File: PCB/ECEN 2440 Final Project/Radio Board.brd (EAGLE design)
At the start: 41.6 x 57.1 mm, 14 parts

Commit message: Final updates to the board
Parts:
- removed U$5: LDO-S-816, Custom Library:LDO-S-816
- added 3V3POWER: (no value), pinhead:1X02
- added LM317: LM317, Custom Library:LM317
- added R4, R5: 100R, rcl:R0805
- moved X1 33.1 mm to (12.7, 85.1)
- moved U$6 31.9 mm to (8.89, 74.9)
- moved U$4 7.73 mm to (5.08, 11.4)
- renumbered JP2 to RADIO, JP3 to BATTERYPOWER
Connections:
- new net N$8: LM317.ADJUST1, R4.1
- net +3V3: now also 3V3POWER.1, LM317.VOUT, R4.2, R5.1
- net GND: now also 3V3POWER.2, R5.2; no longer U$5.VSS
- net VCC: now also LM317.VIN; no longer U$5.VIN
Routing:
- net GND: track 0.00 -> 184.1 mm
- net +3V3: track 0.00 -> 119.0 mm
- net VCC: track 0.00 -> 66.5 mm
- net N$3: track 0.00 -> 48.1 mm, vias 0 -> 1
- net N$1: track 0.00 -> 39.9 mm
- net AUDIO_PWM: track 0.00 -> 38.0 mm
- net AUDIO_PTT: track 0.00 -> 26.4 mm
- net N$5: track 0.00 -> 17.2 mm
- net N$8: track 0.00 -> 14.1 mm
- net N$2: track 0.00 -> 13.0 mm
- net N$4: track 0.00 -> 13.0 mm
- net N$6: track 0.00 -> 10.4 mm
- net RX_RADIO: track 0.00 -> 9.01 mm
- net TX_RADIO: track 0.00 -> 7.14 mm
- net GND1: track 0.00 -> 3.19 mm
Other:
- board size 41.6 x 57.1 mm -> 44.1 x 86.3 mm

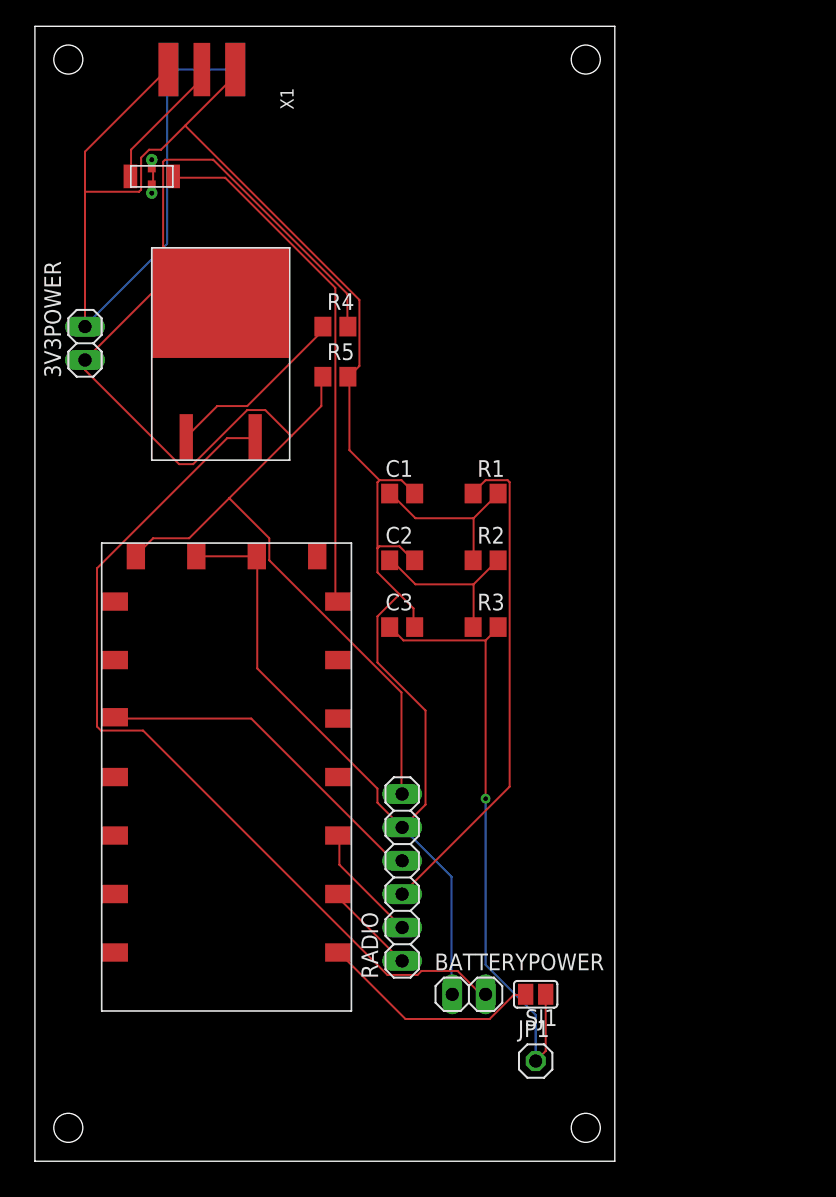
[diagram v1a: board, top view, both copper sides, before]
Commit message: radio board routing
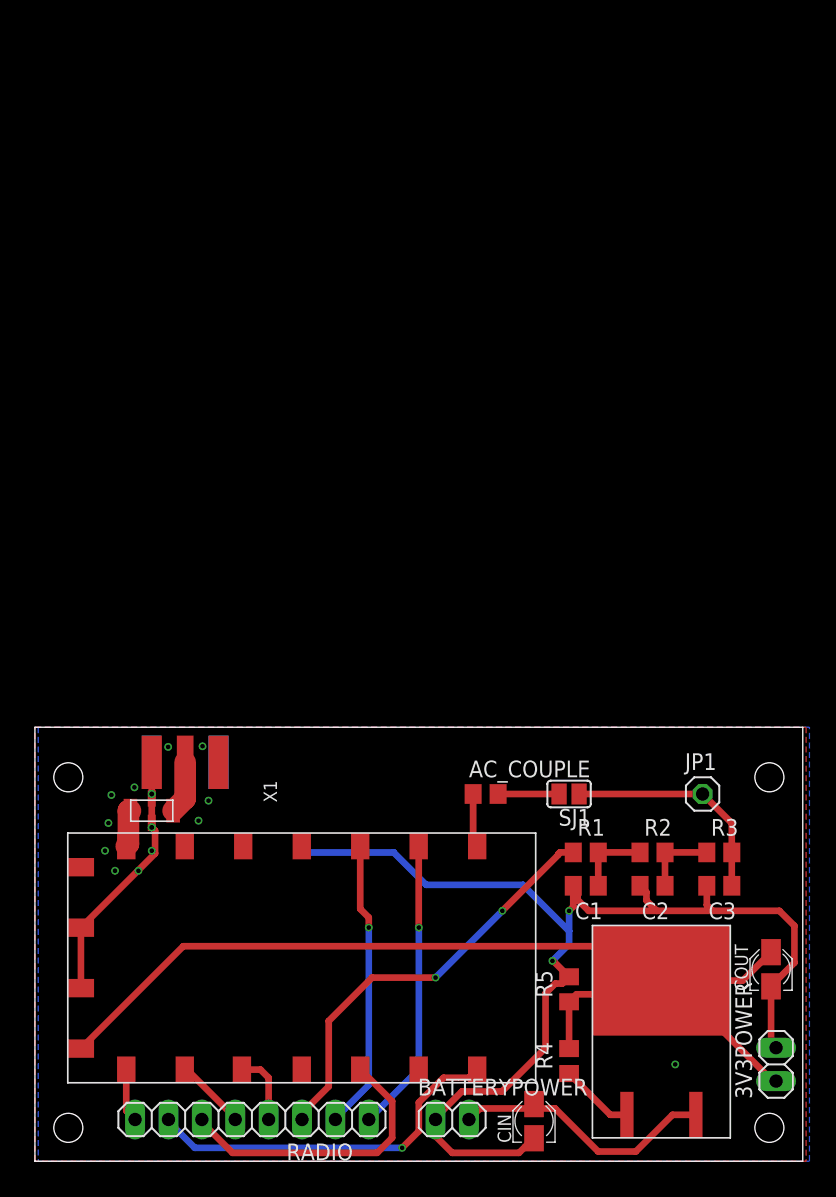
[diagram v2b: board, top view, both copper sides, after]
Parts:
- added AC_COUPLE: 1u, rcl:C0805
- added CIN: 100nF, rcl:PANASONIC_A
- added COUT: 1uF, rcl:PANASONIC_A
- R4: value 100R -> 220R
- R5: value 100R -> 470R
- RADIO: device pinhead:1X06 -> pinhead:1X08
- moved 3V3POWER 76.0 mm to (56.4, 7.37)
- moved LM317 61.5 mm to (42.4, 1.78)
- moved R4 58.6 mm to (40.6, 7.62), turned to 90 degrees
- moved X1 52.7 mm to (11.4, 32.4)
- moved R5 49.9 mm to (40.6, 13.1), turned to 90 degrees
- moved U$6 48.3 mm to (8.89, 26.7), turned to 0 degrees
- moved U$4 33.5 mm to (38.1, 5.97), turned to 90 degrees
- moved C1 33.0 mm to (41.9, 21.0), turned to 180 degrees
- moved C2 31.2 mm to (47.0, 21.0), turned to 180 degrees
- moved C3 31.1 mm to (52.1, 21.0), turned to 180 degrees
- moved R1 28.3 mm to (41.9, 23.5)
- moved R2 25.6 mm to (47.0, 23.5)
- moved R3 24.7 mm to (52.1, 23.5)
- moved JP1 24.0 mm to (50.8, 27.9)
- moved RADIO 21.7 mm to (16.5, 3.17), turned to 180 degrees
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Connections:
- removed net GND1: U$6.GND1, U$6.GND2, U$6.P$1, U$6.P$2
- new net AF_OUT: RADIO.6, U$4.AF_OUT
- new net H/L: RADIO.8, U$4.H/L
- new net N$7: AC_COUPLE.2, SJ1.2
- new net PD: RADIO.5, U$4.PD
- new net SQ: RADIO.7, U$4.SQ
- net +3V3: now also COUT.+; no longer RADIO.6
- net GND: now also CIN.-, COUT.-, U$6.GND1, U$6.GND2, U$6.P$1, U$6.P$2; no longer RADIO.5
- net N$5: now also AC_COUPLE.1; no longer SJ1.2
- net VCC: now also CIN.+
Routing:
- net GND: track 184.1 -> 111.8 mm, vias 0 -> 14
- net VCC: track 66.5 -> 20.6 mm
- net +3V3: track 119.0 -> 80.5 mm
- net N$1: track 39.9 -> 2.92 mm
- net N$3: track 48.1 -> 17.3 mm, vias 1 -> 0
- net SQ: track 0.00 -> 28.2 mm, vias 0 -> 1
- net AF_OUT: track 0.00 -> 22.3 mm
- net AUDIO_PTT: track 26.4 -> 5.46 mm
- net TX_RADIO: track 7.14 -> 22.4 mm, vias 0 -> 1
- net RX_RADIO: track 9.01 -> 22.1 mm, vias 0 -> 1
- net N$5: track 17.2 -> 4.10 mm
- net N$8: track 14.1 -> 5.70 mm
- net N$2: track 13.0 -> 5.72 mm
- net N$4: track 13.0 -> 5.72 mm
- net N$6: track 10.4 -> 4.06 mm
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- added copper zone on layer 1, net GND
- added copper zone on layer 16, net GND
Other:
- board size 44.1 x 86.3 mm -> 58.4 x 33 mm

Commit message: final (before review & order) dra818v breakout board
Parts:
- moved SJ1 3.56 mm to (44.2, 27.9)
- moved AC_COUPLE 2.03 mm to (36.3, 27.9)
- renumbered BATTERYPOWER to BATT
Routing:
- net GND: track 111.8 -> 119.5 mm
- net AUDIO_PWM: track 32.3 -> 35.2 mm
- net N$7: track 4.64 -> 6.16 mm
- net N$3: track 17.3 -> 15.9 mm
- net N$5: track 4.10 -> 5.30 mm
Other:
- board text added: "+"
- board text added: "aout"
- board text added: "h/l"
- board text added: "mic"
- board text added: "pd"
- board text added: "ptt"
- board text added: "rx"
- board text added: "sq"
- board text added: "tx"

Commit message: final (i hope) radio board
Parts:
- removed 3V3POWER: (no value), pinhead:1X02
- removed LM317: LM317, Custom Library:LM317
- added 4VPWR: (no value), pinhead:1X02
- added C4: 500n, rcl:C0805
- added CIN1, CIN2: (no value), rcl:PANASONIC_A
- added L1: (no value), rcl:L3225M
- added R6: 0R, rcl:R0805
- added R8, R9: (no value), rcl:R0805
- added U$1: BD00COAW, Custom Library:HRP5
- R4: value 220R -> 43k
- R5: value 470R -> 10k
- moved COUT 52.5 mm to (3.56, 17.7), turned to 180 degrees
- moved CIN 44.5 mm to (7.11, 35.1), turned to 270 degrees
- moved BATT 43.2 mm to (2.67, 35.1), turned to 270 degrees
- moved R4 41.0 mm to (2.54, 22.9), flipped to the bottom, turned to 180 degrees
- moved R5 40.5 mm to (2.54, 26.7), flipped to the bottom, turned to 180 degrees
- moved RADIO 21.6 mm to (38.1, 3.17)
- moved C3 17.2 mm to (34.9, 22.2), flipped to the bottom, turned to 0 degrees
- moved U$4 16.7 mm to (54.7, 7.37)
- moved U$6 15.2 mm to (23.6, 30.2), turned to 90 degrees
- moved AC_COUPLE 14.3 mm to (50.2, 31.4), turned to 90 degrees
- moved R3 13.5 mm to (38.7, 21.6), flipped to the bottom, turned to 90 degrees
- moved X1 13.3 mm to (23.6, 37.7)
- moved R1 12.5 mm to (38.7, 11.4), flipped to the bottom, turned to 90 degrees
- moved C2 12.3 mm to (35.2, 17.5), flipped to the bottom, turned to 0 degrees
- moved C1 11.4 mm to (34.5, 12.3), flipped to the bottom, turned to 0 degrees
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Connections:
- removed net +3V3: 3V3POWER.1, COUT.+, LM317.VOUT, R4.2, R5.1, U$4.VBAT
- new net ADJ: R4.2, R5.1, U$1.5
- new net GNDA: R6.1, U$6.GND1, U$6.GND2, U$6.P$1, U$6.P$2, X1.GND@1, X1.GND@2, X1.GND@3, X1.GND@4
- new net N$9: CIN1.+, R8.2
- new net V+: 4VPWR.1, C4.1, L1.2, R8.1, R9.1, U$4.VBAT
- new net VO: COUT.+, L1.1, R4.1, U$1.4
- net GND: now also 4VPWR.2, C4.2, CIN1.-, CIN2.-, R6.2, U$1.3, U$1.6; no longer 3V3POWER.2, U$6.GND1, U$6.GND2, U$6.P$1, U$6.P$2, X1.GND@1, X1.GND@2, X1.GND@3, X1.GND@4
- net N$8: now also CIN2.+, R9.2; no longer LM317.ADJUST1, R4.1
- net VCC: now also U$1.1, U$1.2; no longer LM317.VIN
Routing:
- net GND: track 119.5 -> 0.00 mm, vias 14 -> 10
- net +3V3: track 80.5 -> 0.00 mm
- net AUDIO_PWM: track 35.2 -> 8.62 mm, vias 2 -> 0
- net V+: track 0.00 -> 24.7 mm
- net VO: track 0.00 -> 16.6 mm, vias 0 -> 1
- net AF_OUT: track 22.3 -> 9.92 mm, vias 0 -> 1
- net ADJ: track 0.00 -> 10.1 mm, vias 0 -> 1
- net VCC: track 20.6 -> 11.0 mm
- net PD: track 5.49 -> 11.4 mm
- net AUDIO_PTT: track 5.46 -> 9.80 mm
- net H/L: track 4.07 -> 7.77 mm
- net N$8: track 5.70 -> 2.83 mm
- net N$9: track 0.00 -> 2.83 mm
- net SQ: track 28.2 -> 26.4 mm, vias 1 -> 0
- net N$3: track 15.9 -> 17.7 mm
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- added copper zone on layer 1, net GNDA
- added copper zone on layer 16, net GNDA
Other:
- board size 58.4 x 33 mm -> 58.4 x 38.1 mm

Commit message: final board maybe??
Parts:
- U$1: value BD00COAW -> BDXXC0A-CBD00C0AWHFP-CTR
- moved U$1 0.65 mm to (7.62, 25.7)
- moved CIN 0.65 mm to (6.48, 35.2)
- moved C4 0.52 mm to (16.4, 10.9)
- moved R9 0.52 mm to (8.76, 10.9)
- moved R8 0.52 mm to (12.6, 10.9)
- moved R6 0.38 mm to (16.3, 35.4)
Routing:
- net ADJ: track 10.1 -> 8.33 mm
- net AUDIO_PTT: track 9.80 -> 10.6 mm, vias 0 -> 1
- net V+: track 24.7 -> 24.1 mm
- net VCC: track 11.0 -> 10.4 mm
- net N$8: track 2.83 -> 3.39 mm
- net N$9: track 2.83 -> 3.39 mm
- net SQ: track 26.4 -> 25.9 mm
- net N$5: track 5.10 -> 4.60 mm
- net N$1: track 3.25 -> 2.75 mm

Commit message: naming
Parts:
- C1, C2, C3: value 500n -> (none)
- R1, R2, R3: value 100R -> 0R
- renumbered CIN1 to C5, CIN2 to C6
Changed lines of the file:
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@@
 <setting verticaltext="up"/>
 </settings>
-<grid distance="0.05" unitdist="inch" unit="mil" style="lines" multiple="1" display="yes" altdistance="5" altunitdist="mil" altunit="inch"/>
+<grid distance="0.05" unitdist="inch" unit="mm" style="lines" multiple="1" display="yes" altdistance="5" altunitdist="mil" altunit="inch"/>
 <layers>
 <layer number="1" name="Top" color="4" fill="1" visible="yes" active="yes"/>
@@
 </autorouter>
 <elements>
-<element name="C1" library="rcl" library_urn="urn:adsk.eagle:library:334" package="C0805" package3d_urn="urn:adsk.eagle:package:23617/2" value="500n" x="34.544" y="12.319" smashed="yes" rot="MR0">
+<element name="C1" library="rcl" library_urn="urn:adsk.eagle:library:334" package="C0805" package3d_urn="urn:adsk.eagle:package:23617/2" value="" x="34.544" y="12.319" smashed="yes" rot="MR0">
 <attribute name="NAME" x="35.814" y="13.589" size="1.27" layer="26" rot="MR0"/>
 <attribute name="POPULARITY" value="63" x="-2.286" y="-28.321" size="1.778" layer="28" rot="MR0" display="off"/>
@@
 <attribute name="VALUE" x="35.814" y="9.779" size="1.27" layer="28" rot="MR0"/>
 </element>
-<element name="C2" library="rcl" library_urn="urn:adsk.eagle:library:334" package="C0805" package3d_urn="urn:adsk.eagle:package:23617/2" value="500n" x="35.179" y="17.526" smashed="yes" rot="MR0">
+<element name="C2" library="rcl" library_urn="urn:adsk.eagle:library:334" package="C0805" package3d_urn="urn:adsk.eagle:package:23617/2" value="" x="35.179" y="17.526" smashed="yes" rot="MR0">
 <attribute name="NAME" x="36.449" y="18.796" size="1.27" layer="26" rot="MR0"/>
 <attribute name="POPULARITY" value="63" x="-8.001" y="-23.114" size="1.778" layer="28" rot="MR0" display="off"/>
@@
 <attribute name="VALUE" x="36.449" y="14.986" size="1.27" layer="28" rot="MR0"/>
 </element>
-<element name="C3" library="rcl" library_urn="urn:adsk.eagle:library:334" package="C0805" package3d_urn="urn:adsk.eagle:package:23617/2" value="500n" x="34.925" y="22.225" smashed="yes" rot="MR0">
+<element name="C3" library="rcl" library_urn="urn:adsk.eagle:library:334" package="C0805" package3d_urn="urn:adsk.eagle:package:23617/2" value="" x="34.925" y="22.225" smashed="yes" rot="MR0">
 <attribute name="NAME" x="36.195" y="23.495" size="1.27" layer="26" rot="MR0"/>
 <attribute name="POPULARITY" value="63" x="18.415" y="-24.765" size="1.778" layer="28" rot="MR0" display="off"/>
@@
 <attribute name="VALUE" x="45.72" y="6.35" size="1.27" layer="27" rot="R180"/>
 </element>
-<element name="R1" library="rcl" library_urn="urn:adsk.eagle:library:334" package="R0805" package3d_urn="urn:adsk.eagle:package:23553/2" value="100R" x="38.735" y="11.43" smashed="yes" rot="MR90">
+<element name="R1" library="rcl" library_urn="urn:adsk.eagle:library:334" package="R0805" package3d_urn="urn:adsk.eagle:package:23553/2" value="0R" x="38.735" y="11.43" smashed="yes" rot="MR90">
 <attribute name="NAME" x="40.005" y="10.795" size="1.27" layer="26" rot="MR90"/>
 <attribute name="POPULARITY" value="85" x="-1.905" y="29.21" size="1.778" layer="28" rot="MR90" display="off"/>
@@
 <attribute name="VALUE" x="36.195" y="10.795" size="1.27" layer="28" rot="MR90"/>
 </element>
-<element name="R2" library="rcl" library_urn="urn:adsk.eagle:library:334" package="R0805" package3d_urn="urn:adsk.eagle:package:23553/2" value="100R" x="38.735" y="16.51" smashed="yes" rot="MR90">
+<element name="R2" library="rcl" library_urn="urn:adsk.eagle:library:334" package="R0805" package3d_urn="urn:adsk.eagle:package:23553/2" value="0R" x="38.735" y="16.51" smashed="yes" rot="MR90">
 <attribute name="NAME" x="40.005" y="15.875" size="1.27" layer="26" rot="MR90"/>
 <attribute name="POPULARITY" value="85" x="-1.905" y="40.64" size="1.778" layer="28" rot="MR90" display="off"/>
@@
 <attribute name="VALUE" x="36.195" y="15.875" size="1.27" layer="28" rot="MR90"/>
 </element>
-<element name="R3" library="rcl" library_urn="urn:adsk.eagle:library:334" package="R0805" package3d_urn="urn:adsk.eagle:package:23553/2" value="100R" x="38.735" y="21.59" smashed="yes" rot="MR90">
+<element name="R3" library="rcl" library_urn="urn:adsk.eagle:library:334" package="R0805" package3d_urn="urn:adsk.eagle:package:23553/2" value="0R" x="38.735" y="21.59" smashed="yes" rot="MR90">
 <attribute name="NAME" x="40.005" y="20.955" size="1.27" layer="26" rot="MR90"/>
 <attribute name="POPULARITY" value="85" x="-1.905" y="52.07" size="1.778" layer="28" rot="MR90" display="off"/>
@@
 <attribute name="VALUE" x="11.303" y="10.287" size="1.27" layer="27" rot="R90"/>
 </element>
-<element name="CIN1" library="rcl" library_urn="urn:adsk.eagle:library:334" package="PANASONIC_A" package3d_urn="urn:adsk.eagle:package:23418/2" value="" x="12.7" y="16.51" smashed="yes" rot="R270">
+<element name="C5" library="rcl" library_urn="urn:adsk.eagle:library:334" package="PANASONIC_A" package3d_urn="urn:adsk.eagle:package:23418/2" value="" x="12.7" y="16.51" smashed="yes" rot="R270">
 <attribute name="NAME" x="14.45" y="18.16" size="1.016" layer="25" rot="R270"/>
 <attribute name="POPULARITY" value="1" x="12.7" y="16.51" size="1.778" layer="27" rot="R270" display="off"/>
@@
 <attribute name="VALUE" x="9.875" y="18.16" size="1.016" layer="27" rot="R270"/>
 </element>
-<element name="CIN2" library="rcl" library_urn="urn:adsk.eagle:library:334" package="PANASONIC_A" package3d_urn="urn:adsk.eagle:package:23418/2" value="" x="8.89" y="16.51" smashed="yes" rot="R270">
+<element name="C6" library="rcl" library_urn="urn:adsk.eagle:library:334" package="PANASONIC_A" package3d_urn="urn:adsk.eagle:package:23418/2" value="" x="8.89" y="16.51" smashed="yes" rot="R270">
 <attribute name="NAME" x="10.64" y="18.16" size="1.016" layer="25" rot="R270"/>
 <attribute name="POPULARITY" value="1" x="8.89" y="16.51" size="1.778" layer="27" rot="R270" display="off"/>
@@
 <contactref element="COUT" pad="-"/>
 <contactref element="4VPWR" pad="2"/>
-<contactref element="CIN2" pad="-"/>
-<contactref element="CIN1" pad="-"/>
+<contactref element="C6" pad="-"/>
+<contactref element="C5" pad="-"/>
 <contactref element="C4" pad="2"/>
 <via x="10.16" y="36.83" extent="1-16" drill="0.35"/>
@@
 <signal name="N$8">
 <contactref element="R9" pad="2"/>
-<contactref element="CIN2" pad="+"/>
+<contactref element="C6" pad="+"/>
 <wire x1="8.763" y1="15.083" x2="8.89" y2="15.21" width="0.889" layer="1"/>
 <wire x1="8.763" y1="15.083" x2="8.763" y2="11.872" width="0.889" layer="1"/>
@@
 <signal name="N$9">
 <contactref element="R8" pad="2"/>
-<contactref element="CIN1" pad="+"/>
+<contactref element="C5" pad="+"/>
 <wire x1="12.573" y1="15.083" x2="12.7" y2="15.21" width="0.889" layer="1"/>
 <wire x1="12.573" y1="15.083" x2="12.573" y2="11.872" width="0.889" layer="1"/>
